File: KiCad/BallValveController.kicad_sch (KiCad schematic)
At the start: 62 parts, among them J1 Screw_Terminal_01x03, J2 Screw_Terminal_01x04, J3 Screw_Terminal_01x04, J4 Screw_Terminal_01x04, J5 Conn_01x01_Male, J6 Screw_Terminal_01x04, J7 Screw_Terminal_01x02, K1 G5V-2, Q1 Q_PMOS_GDS, Q2 2N2222A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

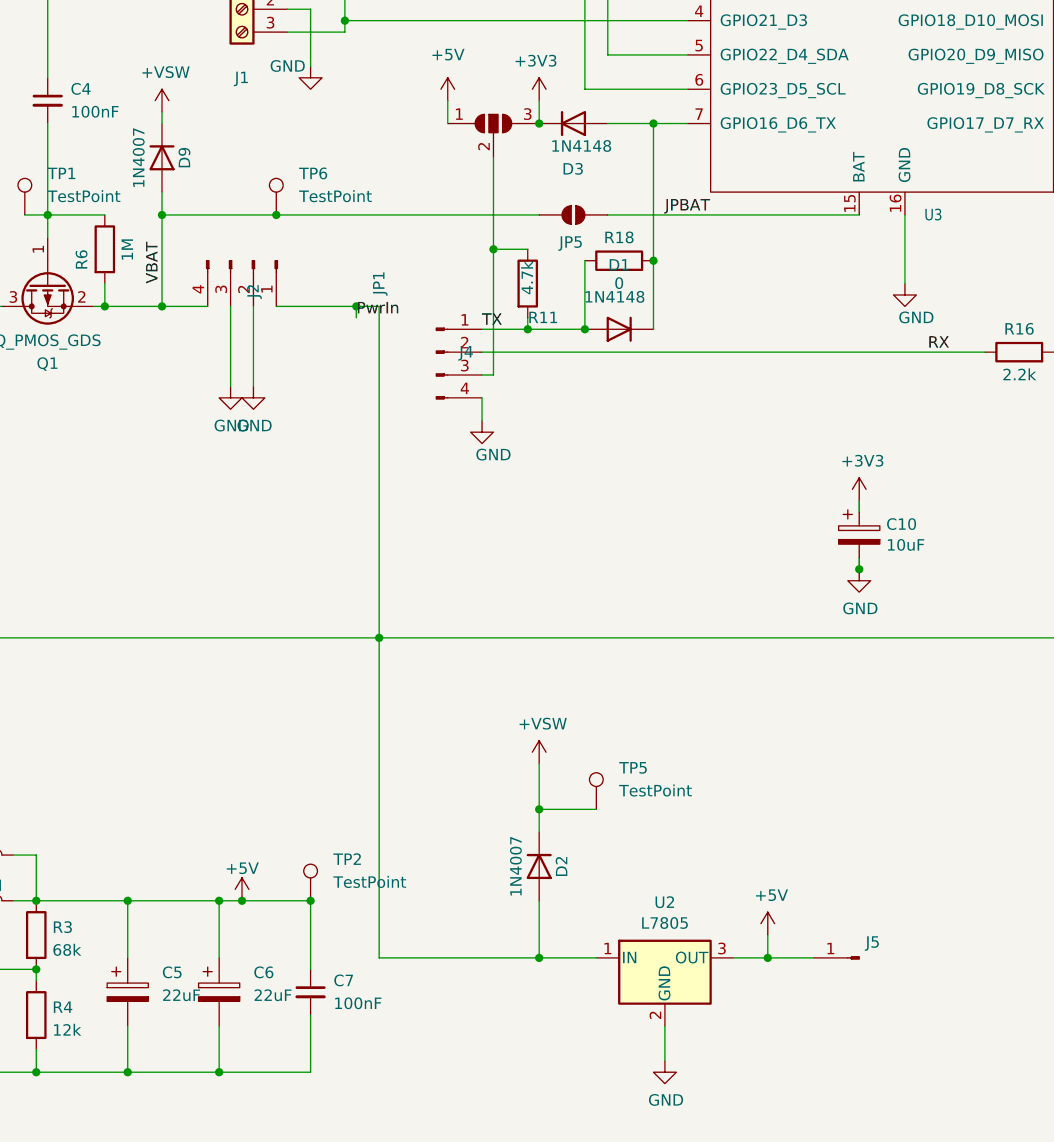
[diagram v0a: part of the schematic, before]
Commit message: Add ME3116 support via 1x3 pin header
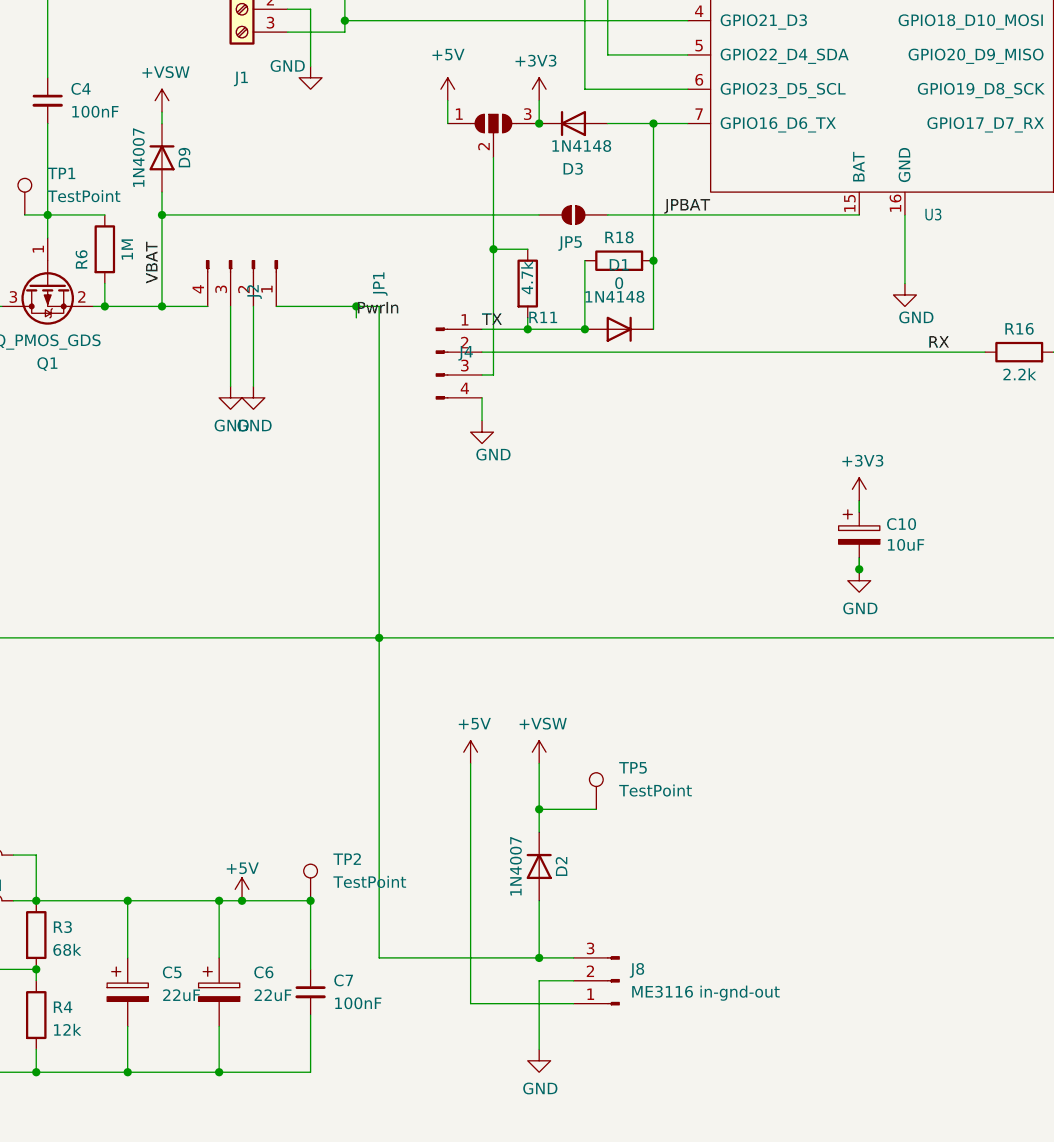
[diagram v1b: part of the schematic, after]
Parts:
- removed J5: Conn_01x01_Male, Connector_PinHeader_2.54mm:PinHeader_1x01_P2.54mm_Vertical, symbol Connector:Conn_01x01_Male
- removed TP6: TestPoint, TestPoint:TestPoint_THTPad_D1.0mm_Drill0.5mm, symbol Connector:TestPoint
- removed U2: L7805, Package_TO_SOT_THT:TO-220-3_Vertical, symbol Regulator_Linear:L7805
- added J8: ME3116 in-gnd-out, Connector_PinHeader_2.54mm:PinHeader_1x03_P2.54mm_Vertical, symbol Connector:Conn_01x03_Pin
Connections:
- net +5V: now also J8.1 (Pin_1)
- net GND: now also J8.2 (Pin_2)
- net PwrIn: now also J8.3 (Pin_3)
